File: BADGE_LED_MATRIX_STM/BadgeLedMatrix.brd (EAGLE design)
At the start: 100 x 50 mm, 110 parts, among them CN2 MICRO-USB-5P-340015001, IC1 STM32F0P, IC2 REG1117, Q1 12MHz, Q2 8MHz, U1 USBLC6SOT-23

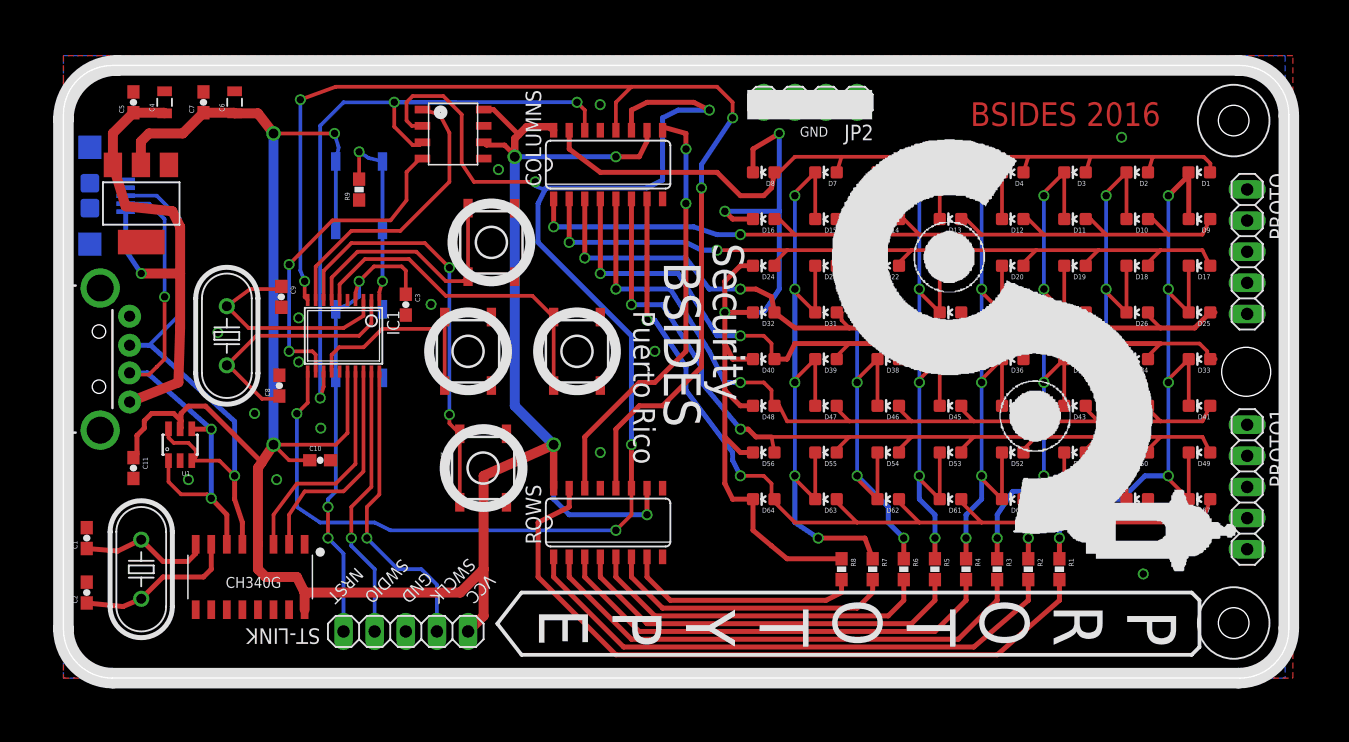
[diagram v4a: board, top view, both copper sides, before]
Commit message: Prototype 2, Ordered. Added EPROM, Slide Switch for PROG
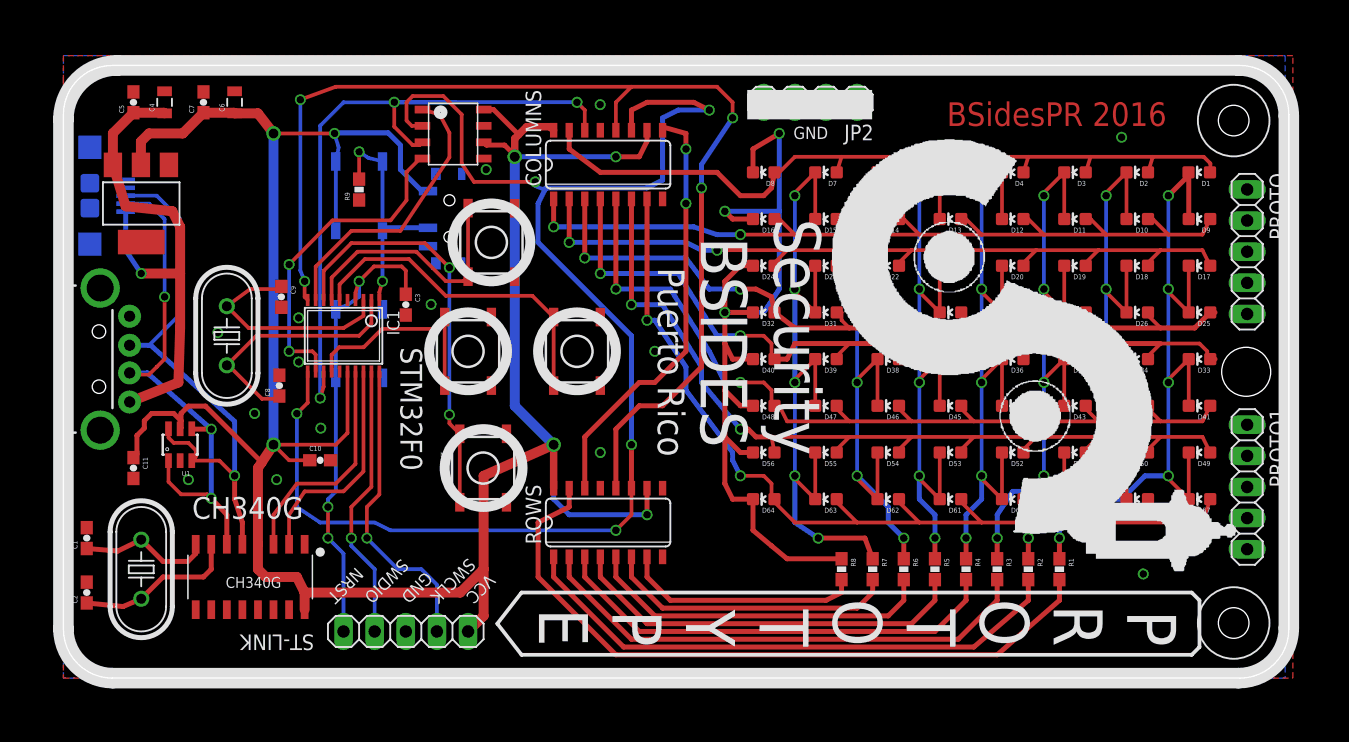
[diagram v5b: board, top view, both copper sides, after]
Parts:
- removed U$4: (no value), logo:RADIOACTIVE
- added S1: (no value), SparkFun-Electromechanical:SWITCH-SPST-SMD-A
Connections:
- net N$4: now also S1.2
- net VCC: now also S1.3
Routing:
- net VCC: track 204.1 -> 214.9 mm
- net N$4: track 15.7 -> 19.5 mm
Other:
- board text added: "@BSidesPR"
- board text added: "BSidesPR 2016"
- board text added: "CH340G"
- board text added: "PROG"
- board text added: "RUN"
- board text added: "STM32F0"
- board text added: "To Program: 1. Connect to PC 2. Slide to PROG 3. Press Reset"
- board text removed: "BSIDES 2016"
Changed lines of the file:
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@@
 <wire x1="92.71" y1="2.54" x2="92.075" y2="1.905" width="0.3048" layer="21"/>
 <wire x1="92.075" y1="1.905" x2="37.385" y2="1.905" width="0.3048" layer="21"/>
-<text x="89.535" y="46.99" size="1.9304" layer="1" font="vector" align="top-right">BSIDES 2016</text>
+<text x="90.035" y="46.99" size="1.9304" layer="1" font="vector" align="top-right">BSidesPR 2016</text>
 <hole x="96.52" y="25" drill="4"/>
 <text x="22.2" y="6" size="1.016" layer="21" rot="SR225" align="top-right">NRST</text>
@@
 <text x="33.5" y="6" size="1.016" layer="21" rot="SR225" align="top-right">VCC</text>
 <rectangle x1="55.8" y1="45.6" x2="66" y2="48" layer="21"/>
-<text x="62.4" y="45" size="0.8128" layer="21" align="top-right">GND</text>
+<text x="62.4" y="45" size="1" layer="21" align="top-right">GND</text>
 <wire x1="100" y1="45.876896875" x2="100" y2="4.10365625" width="1.6764" layer="21"/>
 <wire x1="100" y1="4.10365625" x2="95.89634375" y2="0" width="1.6764" layer="21" curve="-90"/>
@@
 <wire x1="4.386340625" y1="50" x2="95.876896875" y2="50" width="1.6764" layer="22"/>
 <wire x1="95.876896875" y1="50" x2="100" y2="45.876896875" width="1.6764" layer="22" curve="-90"/>
-<text x="53" y="35.5" size="2.54" layer="25" rot="SR270">Security</text>
-<text x="49" y="34" size="3" layer="25" rot="SR270">BSIDES</text>
-<text x="46.5" y="30" size="1.778" layer="25" rot="SR270">Puerto Rico</text>
+<text x="58" y="37.5" size="3.81" layer="25" rot="SR270">Security</text>
+<text x="52" y="36" size="3.81" layer="25" rot="SR270">BSIDES</text>
+<text x="48.5" y="33.5" size="2.1844" layer="25" rot="SR270">Puerto Rico</text>
+<text x="40.5" y="41" size="1.778" layer="22" rot="MR0">PROG</text>
+<text x="34.5" y="33.5" size="1.778" layer="22" rot="MR180">RUN</text>
+<text x="10.5" y="13" size="1.778" layer="21">CH340G</text>
+<text x="27.5" y="27" size="1.778" layer="21" rot="SR270">STM32F0</text>
+<text x="6" y="2.5" size="2.1844" layer="22" rot="SMR90">To Program:
+1. Connect to PC
+2. Slide to PROG
+3. Press Reset</text>
+<wire x1="30.5" y1="44" x2="40.5" y2="44" width="0.4064" layer="22"/>
+<wire x1="40.5" y1="44" x2="42" y2="42.5" width="0.4064" layer="22" curve="-90"/>
+<wire x1="42" y1="42.5" x2="42" y2="32" width="0.4064" layer="22"/>
+<wire x1="42" y1="32" x2="41" y2="31" width="0.4064" layer="22" curve="-90"/>
+<wire x1="41" y1="31" x2="30" y2="31" width="0.4064" layer="22"/>
+<wire x1="30" y1="31" x2="29" y2="32" width="0.4064" layer="22" curve="-90"/>
+<wire x1="29" y1="32" x2="29" y2="42.5" width="0.4064" layer="22"/>
+<wire x1="29" y1="42.5" x2="30.5" y2="44" width="0.4064" layer="22" curve="-90"/>
+<text x="68.5" y="5.5" size="2.54" layer="22" rot="MR180">@BSidesPR</text>
 </plain>
 <attributes>
@@
 </element>
 <element name="R9" library="SparkFun-Passives" package="0603-RES" value="10k" x="24.13" y="39.87" rot="R90"/>
-<element name="PRG" library="SparkFun-Electromechanical" package="TACTILE-SWITCH-SMD" value="SWITCH-MOMENTARY-2SMD-REDUNDANT" x="24.13" y="39.37" rot="MR270"/>
-<element name="RESET" library="SparkFun-Electromechanical" package="TACTILE-SWITCH-SMD" value="SWITCH-MOMENTARY-2SMD-REDUNDANT" x="24.13" y="27.305" rot="MR90"/>
+<element name="PRG" library="SparkFun-Electromechanical" package="TACTILE-SWITCH-SMD" value="SWITCH-MOMENTARY-2SMD-REDUNDANT" x="24.13" y="39.37" smashed="yes" rot="MR270">
+<attribute name="NAME" x="20.852" y="42.759" size="2.1844" layer="26" rot="MR270"/>
+</element>
+<element name="RESET" library="SparkFun-Electromechanical" package="TACTILE-SWITCH-SMD" value="SWITCH-MOMENTARY-2SMD-REDUNDANT" x="24.13" y="27.305" smashed="yes" rot="MR90">
+<attribute name="NAME" x="18.408" y="22.916" size="2.1844" layer="26" rot="MR90"/>
+</element>
 <element name="C3" library="SparkFun-Capacitors" package="0603-CAP" value="22pF" x="27.94" y="30.48" rot="R270"/>
 <element name="ST-LINK" library="pinhead" package="1X05" value="" x="27.94" y="3.81" smashed="yes" rot="R180">
-<attribute name="NAME" x="20.9562" y="4.0612" size="1.27" layer="25" ratio="10" rot="SR180"/>
+<attribute name="NAME" x="20.4562" y="3.5612" size="1.27" layer="25" ratio="10" rot="SR180"/>
 <attribute name="VALUE" x="34.29" y="6.985" size="1.27" layer="27" rot="R180"/>
 </element>
@@
 <element name="U$5" library="special" package="DRIL-2,5" value="" x="95.5" y="45.5"/>
 <element name="U$3" library="special" package="DRIL-2,5" value="" x="95.5" y="4.5"/>
-<element name="U$4" library="logo" package="RADIOACTIVE" value="" x="33.655" y="14.605" rot="MR90"/>
 <element name="CN2" library="Connector" package="B-SMD-5P" value="MICRO-USB-5P-340015001" x="2.54" y="39.37" rot="MR90"/>
 <element name="PROTO" library="pinhead" package="1X05" value="" x="96.6" y="34.8" rot="R270"/>
@@
 <element name="U$1" library="digital-ic" package="OBSIDISLOGO_BOTTOM" value="" x="51.6" y="42.6" rot="R270"/>
 <element name="U$6" library="digital-ic" package="SOP-8" value="AT93C66A" x="31.8" y="44.4"/>
+<element name="S1" library="SparkFun-Electromechanical" package="SWITCH-SPST-SMD-A" value="" x="31.5" y="37.5" rot="MR90"/>
 </elements>
 <signals>
@@
 <via x="43.8" y="46.8" extent="1-16" drill="0.6"/>
 <contactref element="U$6" pad="PIN5"/>
-<via x="35.5" y="41.5" extent="1-16" drill="0.6"/>
+<via x="34.5" y="41.5" extent="1-16" drill="0.6"/>
 <via x="30" y="30.5" extent="1-16" drill="0.6"/>
 </signal>
@@
 <wire x1="34.3" y1="46.4" x2="35.1" y2="46.4" width="0.4064" layer="1"/>
 <wire x1="35.1" y1="46.4" x2="37.15" y2="44.35" width="0.4064" layer="1"/>
+<contactref element="S1" pad="3"/>
+<wire x1="29.75" y1="39.75" x2="29.25" y2="39.75" width="0.4064" layer="16"/>
+<wire x1="29.25" y1="39.75" x2="27.5" y2="41.5" width="0.4064" layer="16"/>
+<wire x1="27.5" y1="41.5" x2="27.5" y2="43.5" width="0.4064" layer="16"/>
+<wire x1="27.5" y1="43.5" x2="26.5" y2="44.5" width="0.4064" layer="16"/>
+<wire x1="26.5" y1="44.5" x2="22.175" y2="44.5" width="0.4064" layer="16"/>
+<wire x1="22.175" y1="44.5" x2="22.125" y2="44.45" width="0.4064" layer="16"/>
 </signal>
 <signal name="C0">
@@
 <wire x1="26.035" y1="42.18" x2="24.9" y2="42.45" width="0.3048" layer="16"/>
 <wire x1="24.9" y1="42.45" x2="24.13" y2="42.95" width="0.3048" layer="16"/>
+<contactref element="S1" pad="2"/>
+<wire x1="29.75" y1="36.75" x2="26.209" y2="36.75" width="0.4064" layer="16"/>
+<wire x1="26.209" y1="36.75" x2="26.035" y2="36.576" width="0.4064" layer="16"/>
 </signal>
 <signal name="NRST">
@@
 <wire x1="20.585" y1="33.585" x2="23.5" y2="36.5" width="0.3048" layer="1"/>
 <wire x1="23.5" y1="36.5" x2="27.5" y2="36.5" width="0.3048" layer="1"/>
-<wire x1="27.5" y1="36.5" x2="31.5" y2="40.5" width="0.3048" layer="1"/>
-<wire x1="31.5" y1="40.5" x2="31.5" y2="44.5" width="0.3048" layer="1"/>
+<wire x1="27.5" y1="36.5" x2="31.5" y2="42.5" width="0.3048" layer="1"/>
+<wire x1="31.5" y1="42.5" x2="31.5" y2="44.5" width="0.3048" layer="1"/>
 <wire x1="31.5" y1="44.5" x2="30.7" y2="46" width="0.3048" layer="1"/>
 <wire x1="30.7" y1="46" x2="29.3" y2="46.4" width="0.3048" layer="1"/>
